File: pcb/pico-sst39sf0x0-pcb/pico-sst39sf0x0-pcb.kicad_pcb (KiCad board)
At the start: 2 copper layers, 101.6 x 54.6 mm, 52 parts, among them Q1 BSS138, Q10 BSS138, Q11 BSS138, Q12 BSS138, Q13 BSS138, Q14 BSS138, Q15 BSS138, Q16 BSS138, Q17 BSS138, Q18 BSS138, Q19 BSS138, Q2 BSS138, Q20 BSS138, Q21 BSS138, Q22 BSS138, Q23 BSS138, Q24 BSS138, Q3 BSS138, Q4 BSS138, Q5 BSS138, Q6 BSS138, Q7 BSS138, Q8 BSS138, Q9 BSS138, SW1 SW_Push, U1 74HC573, U2 SST39SF040, U3 74HC573, U4 Pico, U5 74HC573

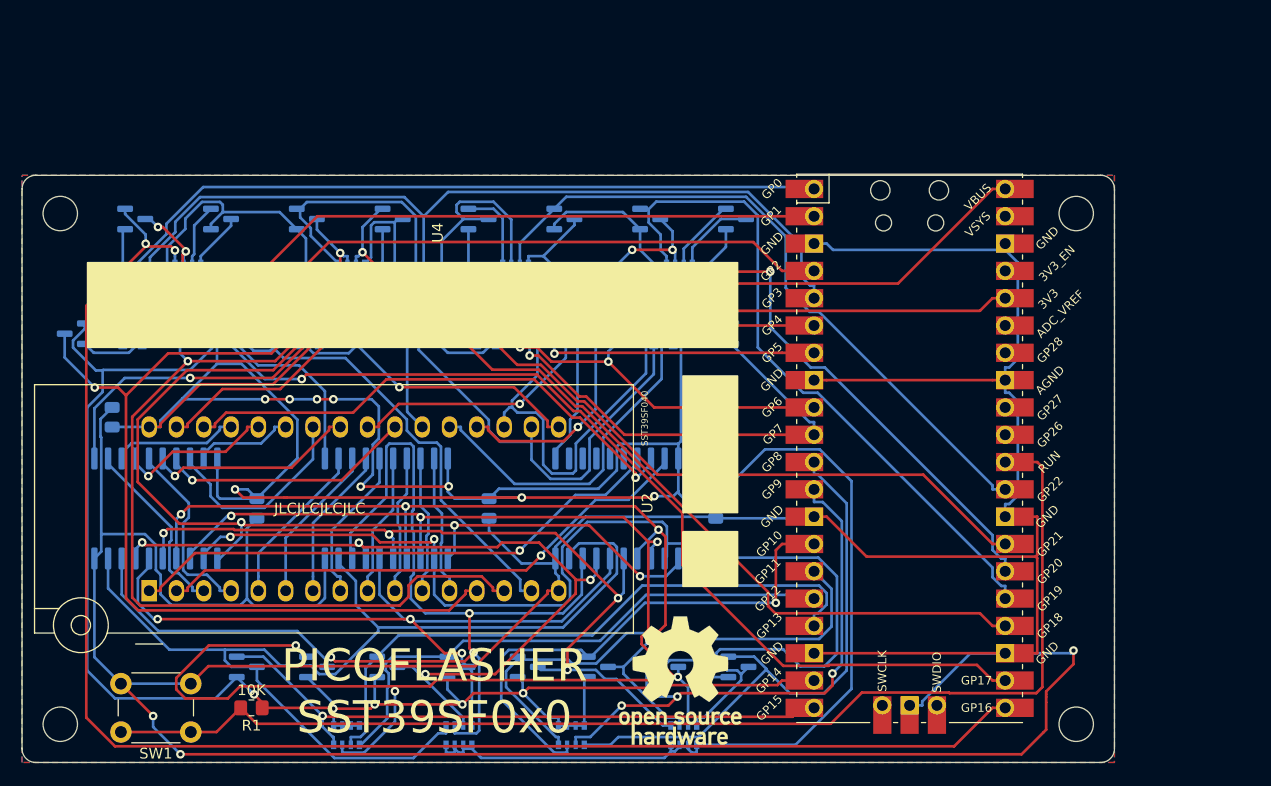
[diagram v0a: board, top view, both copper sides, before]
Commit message: Adding LEDs and putting 10k resistor on backside
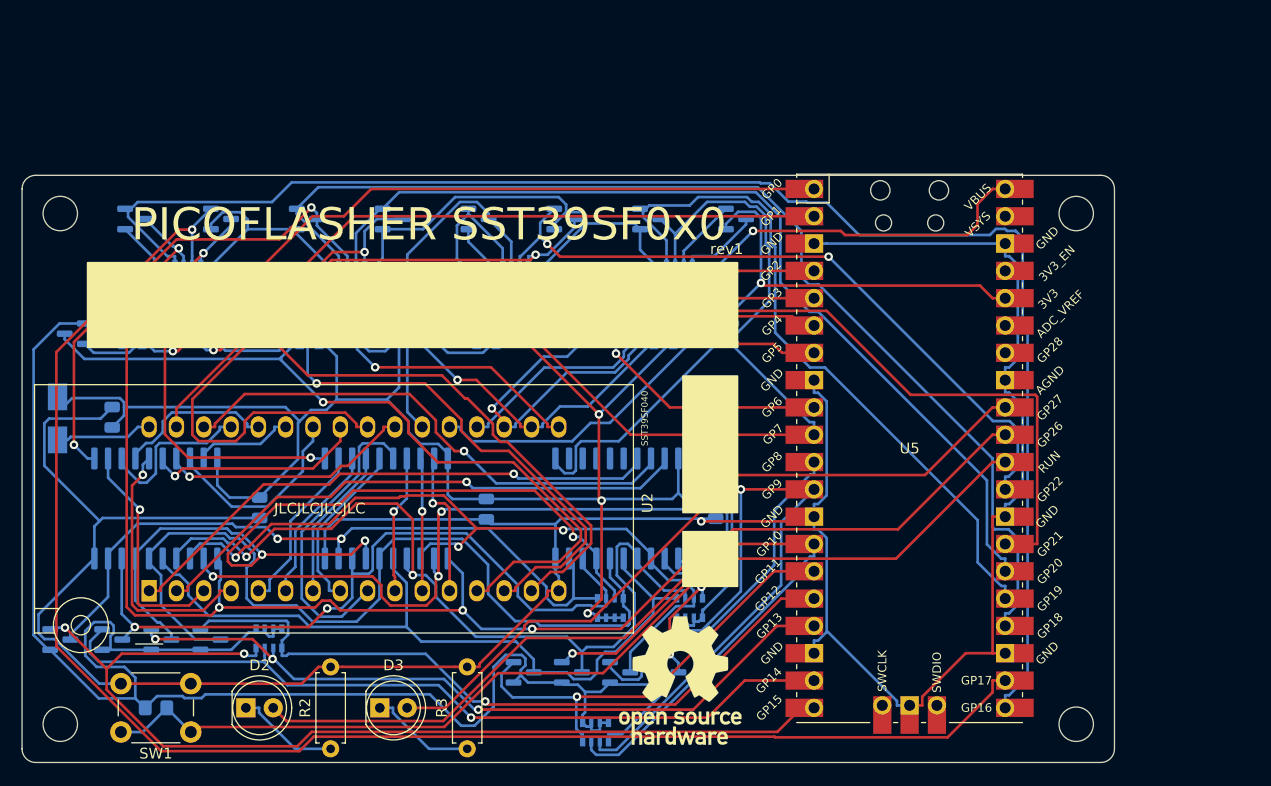
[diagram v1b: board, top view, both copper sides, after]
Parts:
- added D1: M7, Diode_SMD:D_SMA, B.Cu at (17.3, 58.2)
- added D2: LED, LED_THT:LED_D5.0mm, F.Cu at (34.8, 85.1)
- added D3: LED, LED_THT:LED_D5.0mm, F.Cu at (47.2, 85.1)
- added R2: R, Resistor_THT:R_Axial_DIN0207_L6.3mm_D2.5mm_P7.62mm_Horizontal, F.Cu at (42.7, 88.9)
- added R3: R, Resistor_THT:R_Axial_DIN0207_L6.3mm_D2.5mm_P7.62mm_Horizontal, F.Cu at (55.4, 88.9)
- C1, C2, C3, C4: footprint Resistor_SMD:R_0805_2012Metric -> Capacitor_SMD:C_0805_2012Metric
- R1: moved to B.Cu
- moved Q7 23.1 mm to (31.5, 78.7)
- moved Q8 21.2 mm to (26.9, 78.7)
- moved Q9 19.2 mm to (22.4, 78.7)
- moved RN6 18.4 mm to (68.7, 75.8)
- moved Q10 17.5 mm to (17.5, 78.7)
- moved RN3 11.8 mm to (76.1, 75.8)
- moved RN4 11.5 mm to (36.9, 78.6)
- moved R1 8.87 mm to (26.4, 85.1), turned to 0 degrees
- moved Q1 6.53 mm to (74.1, 81.8)
- moved Q2 4.50 mm to (69.6, 81.8)
- moved Q3 2.48 mm to (65.1, 81.8)
- moved RN1 2.26 mm to (67.3, 87.4)
- moved Q4 0.63 mm to (60.6, 81.8)
- moved C3 0.26 mm to (57.1, 66.6)
- moved C2 0.26 mm to (36.1, 66.5)
- renumbered U5 to U4, U4 to U5
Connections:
- U2 pad 32: +5V -> Net-(D1-Pad1)
- U5 pad 31: unconnected-(U4-Pad31) -> GPIO26_3v3
- U5 pad 32: unconnected-(U4-Pad32) -> GPIO27_3v3
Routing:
- net +5V: track 378.2 -> 258.6 mm, vias 12 -> 5
- net GND: track 387.2 -> 267.9 mm, vias 3 -> 1
- net GPIO26_3v3: track 0.00 -> 79.6 mm
- net GPIO27_3v3: track 0.00 -> 67.4 mm
- net LALS: track 103.4 -> 146.3 mm
- net +3V3: track 340.1 -> 378.9 mm, vias 9 -> 1
- net P6: track 103.8 -> 69.1 mm, vias 3 -> 2
- net P7: track 101.1 -> 66.8 mm, vias 0 -> 2
- net LP7: track 59.5 -> 93.6 mm, vias 1 -> 2
- net ~{OE}: track 38.4 -> 66.7 mm
- net P0: track 108.7 -> 84.1 mm, vias 2 -> 5
- net LD3: track 93.1 -> 68.6 mm, vias 0 -> 1
- net AUS: track 30.9 -> 51.7 mm, vias 2 -> 0
- net RUN: track 112.8 -> 94.5 mm
- net LP0: track 54.0 -> 37.2 mm
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- removed copper zone on B.Cu, net +5V
- removed copper zone on F.Cu, net GND
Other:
- board text added: "rev1"

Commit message: Adding polarity protection diode and 10k resistor on backside. Adding LEDS on front side
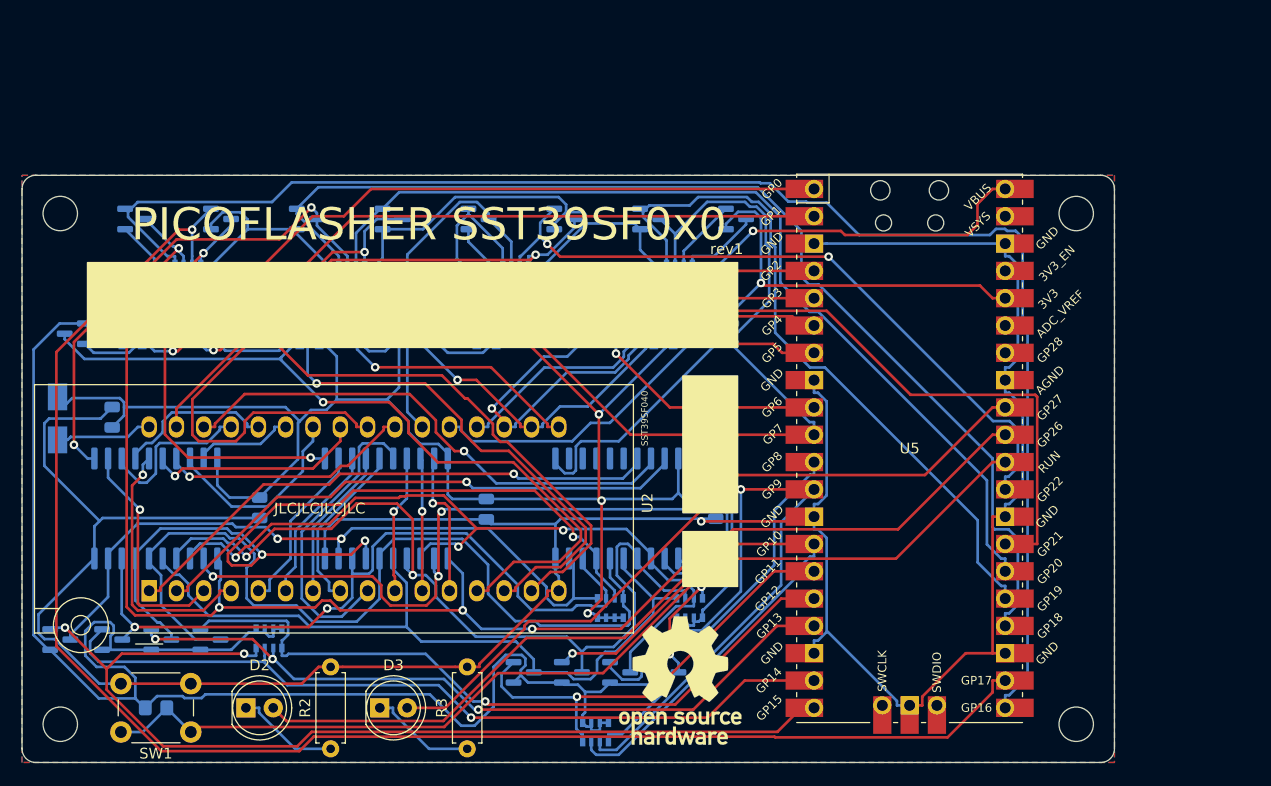
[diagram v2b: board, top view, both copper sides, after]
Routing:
- added copper zone on B.Cu, net +5V
- added copper zone on F.Cu, net GND
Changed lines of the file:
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@@
   (segment (start 75.654 76.708) (end 75.654 77.0706) (width 0.25) (layer "B.Cu") (net 83))
   (segment (start 44.2315 45.604) (end 44.2315 46.2167) (width 0.25) (layer "B.Cu") (net 83))
+  (zone (net 49) (net_name "GND") (layer "F.Cu") (hatch edge 0.508)
+    (connect_pads (clearance 0.508))
+    (min_thickness 0.254) (filled_areas_thickness no)
+    (fill yes (thermal_gap 0.508) (thermal_bridge_width 0.508))
+    (polygon
+      (pts
+        (xy 115.57 90.17)
+        (xy 13.97 90.17)
+        (xy 13.97 35.56)
+        (xy 115.57 35.56)
+      )
+    )
+  )
+  (zone (net 83) (net_name "+5V") (layer "B.Cu") (hatch edge 0.508)
+    (connect_pads (clearance 0.508))
+    (min_thickness 0.254) (filled_areas_thickness no)
+    (fill yes (thermal_gap 0.508) (thermal_bridge_width 0.508))
+    (polygon
+      (pts
+        (xy 115.57 90.17)
+        (xy 13.97 90.17)
+        (xy 13.97 35.56)
+        (xy 115.57 35.56)
+      )
+    )
+  )
 )

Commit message: Revision 2 of the PCB (#11)
* Initial commit revision 2

* Revising top case

* Updating photo

* Updating photos PCBs
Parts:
- R2, R3: value R -> 560; footprint Resistor_THT:R_Axial_DIN0207_L6.3mm_D2.5mm_P7.62mm_Horizontal -> Resistor_SMD:R_0805_2012Metric_Pad1.20x1.40mm_HandSolder; moved to B.Cu
- moved R3 7.88 mm to (55.5, 81.0), turned to 0 degrees
- moved R2 2.67 mm to (42.7, 86.2)
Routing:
- net GND: track 267.9 -> 284.6 mm, vias 1 -> 3
- net Net-(D3-K): track 9.98 -> 11.8 mm, vias 0 -> 1
- net P3: track 70.5 -> 71.2 mm
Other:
- board text added: "rev2"
- board text removed: "rev1"

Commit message: Tweaking lay-out PCB
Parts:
- removed the G1 at (75.2, 82.5)
- added G1: LOGO, components:oshw_certificate_stacked, F.Cu at (33.3, 33.8)
- added G1: Logo_Open_Hardware_Small, Symbol:OSHW-Logo_11.4x12mm_SilkScreen, F.Cu at (87.9, 66.8)
- added G1: LOGO, components:oshw_certificate_stacked, B.Cu at (108.2, 32.8)
- added G4: LOGO, components:raspberry_pi_logo, F.Cu at (107.8, 60.5)
- D2: value LED -> READ
- D3: value LED -> WRITE
- U2: value SST39SF040 -> ZIF SOCKET
- moved C3 18.1 mm to (68.6, 52.6)
- moved H3 18.1 mm to (123.4, 72.6)
- moved H4 18.1 mm to (123.4, 25.1)
- moved Q1 18.1 mm to (85.5, 67.8)
- moved Q22 18.1 mm to (90.4, 36.3)
- moved Q3 18.1 mm to (76.5, 67.8)
- moved RN10 18.1 mm to (68.6, 36.3)
- moved RN12 18.1 mm to (85.1, 36.3)
- moved RN8 18.1 mm to (71.3, 30.7)
- moved U5 18.1 mm to (108.0, 47.0)
- moved C2 18.1 mm to (47.5, 52.5)
- moved D1 18.1 mm to (28.7, 44.2)
- moved D2 18.1 mm to (46.2, 71.1)
- moved D3 18.1 mm to (58.7, 71.1)
- moved H1 18.1 mm to (29.0, 25.1)
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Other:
- board text added: "https://github.com/ifilot/pico-sst39sf0x0-programmer"
- board text added: "rev3"
- board text removed: "rev2"
